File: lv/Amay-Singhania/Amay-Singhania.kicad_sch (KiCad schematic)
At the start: 0 parts

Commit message: created custom strain gauge footprint; added schematic with 1 reference gauge, 1 gauge, and 2 resistors as a wheatstone bridge; created pcb traces for gauge
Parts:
- added R1, R2: 350, Package_DIP:DIP-8_W7.62mm, symbol Device:R
- added S1: StrainGauge, StrainGuage:Strain Guage V1, symbol Device:R_Variable
- added S2: StrainGaugeRef, StrainGuage:Strain Guage V1, symbol Device:R_Variable
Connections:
- new net: R1.1, S1.1
- new net: R2.1, S2.1
- new net +3.3V: S1.2, S2.2
- new net GND: R1.2, R2.2

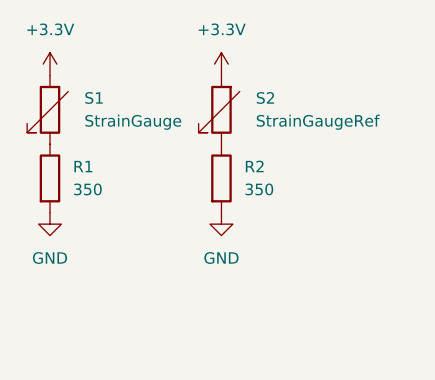
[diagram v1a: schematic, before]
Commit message: edited kicad strain gauge footprint and changed the schematic
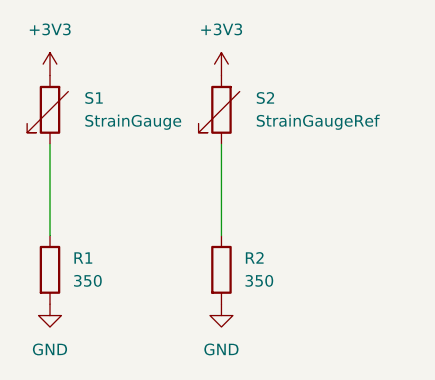
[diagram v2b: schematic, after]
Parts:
- R1, R2: footprint Package_DIP:DIP-8_W7.62mm -> Resistor_SMD:R_01005_0402Metric
- S1, S2: footprint StrainGuage:Strain Guage V1 -> StrainGauge:Strain Gauge V1
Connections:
- net +3.3V renamed +3V3
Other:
- moved on the sheet: R1, R2
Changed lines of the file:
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@@
 		(comment 3 "${COMMENT2}")
+	)
+	(wire
+		(pts
+			(xy 58.42 49.53) (xy 58.42 39.37)
+		)
+		(stroke
+			(width 0)
+			(type default)
+		)
+	)
+	(wire
+		(pts
+			(xy 39.37 49.53) (xy 39.37 39.37)
+		)
+		(stroke
+			(width 0)
+			(type default)
+		)
 	)
 	(symbol
 		(lib_id "Device:R")
-		(at 39.37 43.18 0)
+		(at 39.37 53.34 0)
 		(unit 1)
 		(body_style 1)
@@
 		(fields_autoplaced yes)
 		(property "Reference" "R1"
-			(at 41.91 41.9099 0)
+			(at 41.91 52.0699 0)
 			(show_name no)
 			(do_not_autoplace no)
@@
 		)
 		(property "Value" "350"
-			(at 41.91 44.4499 0)
+			(at 41.91 54.6099 0)
 			(show_name no)
 			(do_not_autoplace no)
@@
 			)
 		)
-		(property "Footprint" "Package_DIP:DIP-8_W7.62mm"
-			(at 37.592 43.18 90)
+		(property "Footprint" "Resistor_SMD:R_01005_0402Metric"
+			(at 37.592 53.34 90)
 			(hide yes)
 			(show_name no)
@@
 		)
 		(property "Datasheet" ""
-			(at 39.37 43.18 0)
+			(at 39.37 53.34 0)
 			(hide yes)
 			(show_name no)
@@
 		)
 		(property "Description" "Resistor"
-			(at 39.37 43.18 0)
+			(at 39.37 53.34 0)
 			(hide yes)
 			(show_name no)
@@
 		)
 		(property "Digikey Part Number" ""
-			(at 39.37 43.18 0)
+			(at 39.37 53.34 0)
 			(hide yes)
 			(show_name no)
@@
 		)
 		(property "Digikey URL" ""
-			(at 39.37 43.18 0)
+			(at 39.37 53.34 0)
 			(hide yes)
 			(show_name no)
@@
 		)
 		(property "Manufacturer" ""
-			(at 39.37 43.18 0)
+			(at 39.37 53.34 0)
 			(hide yes)
 			(show_name no)
@@
 		)
 		(property "Manufacturer Part Number" ""
-			(at 39.37 43.18 0)
+			(at 39.37 53.34 0)
 			(hide yes)
 			(show_name no)
@@
 	(symbol
 		(lib_id "power:GND")
-		(at 39.37 46.99 0)
+		(at 39.37 57.15 0)
 		(unit 1)
 		(body_style 1)
@@
 		(fields_autoplaced yes)
 		(property "Reference" "#PWR02"
-			(at 39.37 53.34 0)
+			(at 39.37 63.5 0)
 			(hide yes)
 			(show_name no)
@@
 		)
 		(property "Value" "GND"
-			(at 39.37 52.07 0)
+			(at 39.37 62.23 0)
 			(show_name no)
 			(do_not_autoplace no)
@@
 		)
 		(property "Footprint" ""
-			(at 39.37 46.99 0)
+			(at 39.37 57.15 0)
 			(hide yes)
 			(show_name no)
@@
 		)
 		(property "Datasheet" ""
-			(at 39.37 46.99 0)
+			(at 39.37 57.15 0)
 			(hide yes)
 			(show_name no)
@@
 		)
 		(property "Description" "Power symbol creates a global label with name \"GND\" , ground"
-			(at 39.37 46.99 0)
+			(at 39.37 57.15 0)
 			(hide yes)
 			(show_name no)
@@
 			)
 		)
-		(property "Footprint" "StrainGuage:Strain Guage V1"
+		(property "Footprint" "StrainGauge:Strain Gauge V1"
 			(at 60.198 35.56 90)
 			(hide yes)
@@
 	(symbol
 		(lib_id "power:GND")
-		(at 58.42 46.99 0)
+		(at 58.42 57.15 0)
 		(unit 1)
 		(body_style 1)
@@
 		(fields_autoplaced yes)
 		(property "Reference" "#PWR04"
-			(at 58.42 53.34 0)
+			(at 58.42 63.5 0)
 			(hide yes)
 			(show_name no)
@@
 		)
 		(property "Value" "GND"
-			(at 58.42 52.07 0)
+			(at 58.42 62.23 0)
 			(show_name no)
 			(do_not_autoplace no)
@@
 		)
 		(property "Footprint" ""
-			(at 58.42 46.99 0)
+			(at 58.42 57.15 0)
 			(hide yes)
 			(show_name no)
@@
 		)
 		(property "Datasheet" ""
-			(at 58.42 46.99 0)
+			(at 58.42 57.15 0)
 			(hide yes)
 			(show_name no)
@@
 		)
 		(property "Description" "Power symbol creates a global label with name \"GND\" , ground"
-			(at 58.42 46.99 0)
+			(at 58.42 57.15 0)
 			(hide yes)
 			(show_name no)
@@
 	)
 	(symbol
-		(lib_id "power:+3.3V")
+		(lib_id "power:+3V3")
 		(at 39.37 31.75 0)
 		(unit 1)
@@
 		(dnp no)
 		(fields_autoplaced yes)
-		(property "Reference" "#PWR01"
+		(property "Reference" "#PWR05"
 			(at 39.37 35.56 0)
 			(hide yes)
@@
 			)
 		)
-		(property "Value" "+3.3V"
+		(property "Value" "+3V3"
 			(at 39.37 26.67 0)
 			(show_name no)
@@
 			)
 		)
-		(property "Description" "Power symbol creates a global label with name \"+3.3V\""
+		(property "Description" "Power symbol creates a global label with name \"+3V3\""
 			(at 39.37 31.75 0)
 			(hide yes)
@@
 			(project "Amay-Singhania"
 				(path "/e994741c-7c7d-4124-9d00-43b883baa61d"
-					(reference "#PWR01")
+					(reference "#PWR05")
+					(unit 1)
+				)
+			)
+		)
+	)
+	(symbol
+		(lib_id "power:+3V3")
+		(at 58.42 31.75 0)
+		(unit 1)
+		(body_style 1)
+		(exclude_from_sim no)
+		(in_bom yes)
+		(on_board yes)
+		(in_pos_files yes)
+		(dnp no)
+		(fields_autoplaced yes)
+		(property "Reference" "#PWR06"
+			(at 58.42 35.56 0)
+			(hide yes)
+			(show_name no)
+			(do_not_autoplace no)
+			(effects
+				(font
+					(size 1.27 1.27)
+				)
+			)
+		)
+		(property "Value" "+3V3"
+			(at 58.42 26.67 0)
+			(show_name no)
+			(do_not_autoplace no)
+			(effects
+				(font
+					(size 1.27 1.27)
+				)
+			)
+		)
+		(property "Footprint" ""
+			(at 58.42 31.75 0)
+			(hide yes)
+			(show_name no)
+			(do_not_autoplace no)
+			(effects
+				(font
+					(size 1.27 1.27)
+				)
+			)
+		)
+		(property "Datasheet" ""
+			(at 58.42 31.75 0)
+			(hide yes)
+			(show_name no)
+			(do_not_autoplace no)
+			(effects
+				(font
+					(size 1.27 1.27)
+				)
+			)
+		)
+		(property "Description" "Power symbol creates a global label with name \"+3V3\""
+			(at 58.42 31.75 0)
+			(hide yes)
+			(show_name no)
+			(do_not_autoplace no)
+			(effects
+				(font
+					(size 1.27 1.27)
+				)
+			)
+		)
+		(pin "1"
+		)
+		(instances
+			(project "Amay-Singhania"
+				(path "/e994741c-7c7d-4124-9d00-43b883baa61d"
+					(reference "#PWR06")
 					(unit 1)
 				)
@@
 			)
 		)
-		(property "Footprint" "StrainGuage:Strain Guage V1"
+		(property "Footprint" "StrainGauge:Strain Gauge V1"
 			(at 41.148 35.56 90)
 			(hide yes)
@@
 	)
 	(symbol
-		(lib_id "power:+3.3V")
-		(at 58.42 31.75 0)
-		(unit 1)
-		(body_style 1)
-		(exclude_from_sim no)
-		(in_bom yes)
-		(on_board yes)
-		(in_pos_files yes)
-		(dnp no)
-		(fields_autoplaced yes)
-		(property "Reference" "#PWR03"
-			(at 58.42 35.56 0)
-			(hide yes)
-			(show_name no)
-			(do_not_autoplace no)
-			(effects
-				(font
-					(size 1.27 1.27)
-				)
-			)
-		)
-		(property "Value" "+3.3V"
-			(at 58.42 26.67 0)
-			(show_name no)
-			(do_not_autoplace no)
-			(effects
-				(font
-					(size 1.27 1.27)
-				)
-			)
-		)
-		(property "Footprint" ""
-			(at 58.42 31.75 0)
-			(hide yes)
-			(show_name no)
-			(do_not_autoplace no)
-			(effects
-				(font
-					(size 1.27 1.27)
-				)
-			)
-		)
-		(property "Datasheet" ""
-			(at 58.42 31.75 0)
-			(hide yes)
-			(show_name no)
-			(do_not_autoplace no)
-			(effects
-				(font
-					(size 1.27 1.27)
-				)
-			)
-		)
-		(property "Description" "Power symbol creates a global label with name \"+3.3V\""
-			(at 58.42 31.75 0)
-			(hide yes)
-			(show_name no)
-			(do_not_autoplace no)
-			(effects
-				(font
-					(size 1.27 1.27)
-				)
-			)
-		)
-		(pin "1"
-		)
-		(instances
-			(project "Amay-Singhania"
-				(path "/e994741c-7c7d-4124-9d00-43b883baa61d"
-					(reference "#PWR03")
-					(unit 1)
-				)
-			)
-		)
-	)
-	(symbol
 		(lib_id "Device:R")
-		(at 58.42 43.18 0)
+		(at 58.42 53.34 0)
 		(unit 1)
 		(body_style 1)
@@
 		(fields_autoplaced yes)
 		(property "Reference" "R2"
-			(at 60.96 41.9099 0)
+			(at 60.96 52.0699 0)
 			(show_name no)
 			(do_not_autoplace no)
@@
 		)
 		(property "Value" "350"
-			(at 60.96 44.4499 0)
+			(at 60.96 54.6099 0)
 			(show_name no)
 			(do_not_autoplace no)
@@
 			)
 		)
-		(property "Footprint" "Package_DIP:DIP-8_W7.62mm"
-			(at 56.642 43.18 90)
+		(property "Footprint" "Resistor_SMD:R_01005_0402Metric"
+			(at 56.642 53.34 90)
 			(hide yes)
 			(show_name no)
@@
 		)
 		(property "Datasheet" ""
-			(at 58.42 43.18 0)
+			(at 58.42 53.34 0)
 			(hide yes)
 			(show_name no)
@@
 		)
 		(property "Description" "Resistor"
-			(at 58.42 43.18 0)
-			(hide yes)
-			(show_name no)
+			(at 58.42 53.34 0)
+			(hide yes)
+			(show_name no)
+			(do_not_autoplace no)
+			(effects
+				(font
+					(size 1.27 1.27)
+				)
+			)
+		)
+		(property "Digikey Part Number" ""
+			(at 58.42 53.34 0)
+			(hide yes)
+			(show_name no)
+			(do_not_autoplace no)
+			(effects
+				(font
+					(size 1.27 1.27)
+				)
+			)
+		)
+		(property "Digikey URL" ""
+			(at 58.42 53.34 0)
+			(hide yes)
+			(show_name no)
+			(do_not_autoplace no)
+			(effects
+				(font
+					(size 1.27 1.27)
+				)
+			)
+		)
+		(property "Manufacturer" ""
+			(at 58.42 53.34 0)
+			(hide yes)
+			(show_name no)
+			(do_not_autoplace no)
+			(effects
+				(font
+					(size 1.27 1.27)
+				)
+			)
+		)
+		(property "Manufacturer Part Number" ""
+			(at 58.42 53.34 0)
+			(hide yes)
+			(show_name no)
